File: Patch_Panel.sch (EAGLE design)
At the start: 43 parts, among them M1_IN APP_2POS_CONFIGMOCO_VERT, M1_OUT APP_2POS_CONFIGMOCO_VERT_DUMMY, M2_IN APP_2POS_CONFIGMOCO_VERT, M2_OUT APP_2POS_CONFIGMOCO_VERT_DUMMY, M3_IN APP_2POS_CONFIGMOCO_VERT, M3_OUT APP_2POS_CONFIGMOCO_VERT_DUMMY, M4_IN APP_2POS_CONFIGMOCO_VERT, M4_OUT APP_2POS_CONFIGMOCO_VERT_DUMMY, M5_IN APP_2POS_CONFIGMOCO_VERT, M5_OUT APP_2POS_CONFIGMOCO_VERT_DUMMY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

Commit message: added cutout, rerouted w/ vert app connectors for power in
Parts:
- added U$22, U$29, U$30, U$31, U$32, U$33, U$34, U$35, U$36, U$37, U$38, U$39, U$40, U$41, U$42, U$43, U$44, U$45: APP_MOUTING_WINGVERT, MRDT-Connectors:APP_MOUTING_WINGVERT
- added U$46: RJ45_PASSTHRUSTEWART-SS82000002, MRDT-Connectors:RJ45_PASSTHRUSTEWART-SS82000002
- U$25, U$26: value ANDERSON_POWERPOLEPP45_PCB_VERT -> APP_2POS_CONFIGMOCO_VERT; device MRDT-Connectors:ANDERSON_POWERPOLEPP45_PCB_VERT -> MRDT-Connectors:APP_2POS_CONFIGMOCO_VERT
- U$27, U$28: value ANDERSON_POWERPOLEPP45_PCB_VERT -> APP_MOUTING_WINGVERT; device MRDT-Connectors:ANDERSON_POWERPOLEPP45_PCB_VERT -> MRDT-Connectors:APP_MOUTING_WINGVERT
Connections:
- net 12V: now also U$25VCC.P$1; no longer U$27.P$1
- net 5V: now also U$26VCC.P$1; no longer U$28.P$1
- net GND: now also U$25GND.P$1, U$26GND.P$1; no longer U$25.P$1, U$26.P$1
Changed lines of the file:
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@@
 <part name="SUPPLY4" library="SparkFun-Aesthetics" deviceset="12V" device=""/>
 <part name="GND2" library="SparkFun-Aesthetics" deviceset="GND" device=""/>
-<part name="U$25" library="MRDT-Connectors" deviceset="ANDERSON_POWERPOLE" device="PP45_PCB_VERT"/>
-<part name="U$26" library="MRDT-Connectors" deviceset="ANDERSON_POWERPOLE" device="PP45_PCB_VERT"/>
-<part name="U$27" library="MRDT-Connectors" deviceset="ANDERSON_POWERPOLE" device="PP45_PCB_VERT"/>
-<part name="U$28" library="MRDT-Connectors" deviceset="ANDERSON_POWERPOLE" device="PP45_PCB_VERT"/>
 <part name="U$8" library="MRDT-Connectors" deviceset="APP_3POS_CONFIG" device="5V_12V_VERT"/>
 <part name="U$1" library="MRDT-Connectors" deviceset="APP_3POS_CONFIG" device="5V_12V_VERT"/>
@@
 <part name="U$20" library="MRDT-Connectors" deviceset="APP_3POS_CONFIG" device="5V_12V_VERT"/>
 <part name="U$21" library="MRDT-Connectors" deviceset="APP_3POS_CONFIG" device="5V_12V_VERT"/>
+<part name="U$22" library="MRDT-Connectors" deviceset="APP_MOUTING_WING" device="VERT"/>
+<part name="U$29" library="MRDT-Connectors" deviceset="APP_MOUTING_WING" device="VERT"/>
+<part name="U$30" library="MRDT-Connectors" deviceset="APP_MOUTING_WING" device="VERT"/>
+<part name="U$31" library="MRDT-Connectors" deviceset="APP_MOUTING_WING" device="VERT"/>
+<part name="U$32" library="MRDT-Connectors" deviceset="APP_MOUTING_WING" device="VERT"/>
+<part name="U$33" library="MRDT-Connectors" deviceset="APP_MOUTING_WING" device="VERT"/>
+<part name="U$34" library="MRDT-Connectors" deviceset="APP_MOUTING_WING" device="VERT"/>
+<part name="U$25" library="MRDT-Connectors" deviceset="APP_2POS_CONFIG" device="MOCO_VERT"/>
+<part name="U$26" library="MRDT-Connectors" deviceset="APP_2POS_CONFIG" device="MOCO_VERT"/>
+<part name="U$27" library="MRDT-Connectors" deviceset="APP_MOUTING_WING" device="VERT"/>
+<part name="U$28" library="MRDT-Connectors" deviceset="APP_MOUTING_WING" device="VERT"/>
+<part name="U$35" library="MRDT-Connectors" deviceset="APP_MOUTING_WING" device="VERT"/>
+<part name="U$36" library="MRDT-Connectors" deviceset="APP_MOUTING_WING" device="VERT"/>
+<part name="U$37" library="MRDT-Connectors" deviceset="APP_MOUTING_WING" device="VERT"/>
+<part name="U$38" library="MRDT-Connectors" deviceset="APP_MOUTING_WING" device="VERT"/>
+<part name="U$39" library="MRDT-Connectors" deviceset="APP_MOUTING_WING" device="VERT"/>
+<part name="U$40" library="MRDT-Connectors" deviceset="APP_MOUTING_WING" device="VERT"/>
+<part name="U$41" library="MRDT-Connectors" deviceset="APP_MOUTING_WING" device="VERT"/>
+<part name="U$42" library="MRDT-Connectors" deviceset="APP_MOUTING_WING" device="VERT"/>
+<part name="U$43" library="MRDT-Connectors" deviceset="APP_MOUTING_WING" device="VERT"/>
+<part name="U$44" library="MRDT-Connectors" deviceset="APP_MOUTING_WING" device="VERT"/>
+<part name="U$45" library="MRDT-Connectors" deviceset="APP_MOUTING_WING" device="VERT"/>
+<part name="U$46" library="MRDT-Connectors" deviceset="RJ45_PASSTHRU" device="STEWART-SS82000002"/>
 </parts>
 <sheets>
@@
 <wire x1="228.6" y1="162.56" x2="228.6" y2="91.44" width="0.1524" layer="94" style="shortdash"/>
 <wire x1="228.6" y1="91.44" x2="86.36" y2="91.44" width="0.1524" layer="94" style="shortdash"/>
-<wire x1="86.36" y1="91.44" x2="86.36" y2="-73.66" width="0.1524" layer="94" style="shortdash"/>
-<wire x1="86.36" y1="-73.66" x2="-25.4" y2="-73.66" width="0.1524" layer="94" style="shortdash"/>
-<wire x1="-25.4" y1="-73.66" x2="-25.4" y2="162.56" width="0.1524" layer="94" style="shortdash"/>
+<wire x1="86.36" y1="91.44" x2="86.36" y2="-231.14" width="0.1524" layer="94" style="shortdash"/>
+<wire x1="86.36" y1="-231.14" x2="-25.4" y2="-231.14" width="0.1524" layer="94" style="shortdash"/>
+<wire x1="-25.4" y1="-231.14" x2="-25.4" y2="162.56" width="0.1524" layer="94" style="shortdash"/>
 <text x="-22.86" y="157.48" size="1.778" layer="94">POWER OUT</text>
 </plain>
@@
 <instance part="SUPPLY4" gate="G$1" x="-7.62" y="205.74"/>
 <instance part="GND2" gate="1" x="7.62" y="208.28" rot="R180"/>
-<instance part="U$25" gate="G$1" x="20.32" y="175.26"/>
-<instance part="U$26" gate="G$1" x="20.32" y="190.5"/>
-<instance part="U$27" gate="G$1" x="20.32" y="195.58"/>
-<instance part="U$28" gate="G$1" x="20.32" y="180.34"/>
 <instance part="U$8" gate="GND" x="20.32" y="139.7"/>
 <instance part="U$8" gate="5V" x="20.32" y="144.78"/>
@@
 <instance part="AUX2_OUT" gate="GND" x="210.82" y="149.86" rot="R270"/>
 <instance part="AUX2_OUT" gate="VCC" x="215.9" y="149.86" rot="R270"/>
-<instance part="U$9" gate="G$1" x="93.98" y="83.82"/>
-<instance part="U$10" gate="G$1" x="93.98" y="76.2"/>
+<instance part="U$9" gate="G$1" x="91.44" y="81.28"/>
+<instance part="U$10" gate="G$1" x="91.44" y="73.66"/>
 <instance part="U$11" gate="GND" x="20.32" y="-73.66"/>
 <instance part="U$11" gate="5V" x="20.32" y="-68.58"/>
@@
 <instance part="U$21" gate="5V" x="20.32" y="-210.82"/>
 <instance part="U$21" gate="12V" x="20.32" y="-205.74"/>
+<instance part="U$22" gate="G$1" x="91.44" y="66.04"/>
+<instance part="U$29" gate="G$1" x="104.14" y="66.04"/>
+<instance part="U$30" gate="G$1" x="104.14" y="73.66"/>
+<instance part="U$31" gate="G$1" x="104.14" y="81.28"/>
+<instance part="U$32" gate="G$1" x="116.84" y="81.28"/>
+<instance part="U$33" gate="G$1" x="116.84" y="73.66"/>
+<instance part="U$34" gate="G$1" x="116.84" y="66.04"/>
+<instance part="U$25" gate="GND" x="20.32" y="190.5"/>
+<instance part="U$25" gate="VCC" x="20.32" y="195.58"/>
+<instance part="U$26" gate="GND" x="20.32" y="175.26"/>
+<instance part="U$26" gate="VCC" x="20.32" y="180.34"/>
+<instance part="U$27" gate="G$1" x="91.44" y="58.42"/>
+<instance part="U$28" gate="G$1" x="91.44" y="50.8"/>
+<instance part="U$35" gate="G$1" x="91.44" y="43.18"/>
+<instance part="U$36" gate="G$1" x="104.14" y="43.18"/>
+<instance part="U$37" gate="G$1" x="104.14" y="50.8"/>
+<instance part="U$38" gate="G$1" x="104.14" y="58.42"/>
+<instance part="U$39" gate="G$1" x="116.84" y="58.42"/>
+<instance part="U$40" gate="G$1" x="116.84" y="50.8"/>
+<instance part="U$41" gate="G$1" x="116.84" y="43.18"/>
+<instance part="U$42" gate="G$1" x="91.44" y="35.56"/>
+<instance part="U$43" gate="G$1" x="104.14" y="35.56"/>
+<instance part="U$44" gate="G$1" x="116.84" y="35.56"/>
+<instance part="U$45" gate="G$1" x="91.44" y="27.94"/>
+<instance part="U$46" gate="G$1" x="91.44" y="12.7"/>
 </instances>
 <busses>
@@
 <wire x1="0" y1="-50.8" x2="0" y2="-33.02" width="0.1524" layer="91"/>
 <pinref part="U$8" gate="5V" pin="P$1"/>
-<pinref part="U$28" gate="G$1" pin="P$1"/>
 <wire x1="0" y1="-33.02" x2="0" y2="-15.24" width="0.1524" layer="91"/>
 <wire x1="0" y1="-15.24" x2="0" y2="2.54" width="0.1524" layer="91"/>
@@
 <junction x="0" y="-68.58"/>
 <junction x="0" y="-50.8"/>
-<wire x1="0" y1="-210.82" x2="0" y2="-195.58" width="0.1524" layer="91"/>
+<wire x1="0" y1="-210.82" x2="0" y2="-193.04" width="0.1524" layer="91"/>
 <wire x1="12.7" y1="-210.82" x2="0" y2="-210.82" width="0.1524" layer="91"/>
 <pinref part="U$21" gate="5V" pin="P$1"/>
-<wire x1="0" y1="-195.58" x2="0" y2="-193.04" width="0.1524" layer="91"/>
 <junction x="0" y="-193.04"/>
+<pinref part="U$26" gate="VCC" pin="P$1"/>
 </segment>
 </net>
@@
 <wire x1="12.7" y1="149.86" x2="-7.62" y2="149.86" width="0.1524" layer="91"/>
 <pinref part="U$8" gate="12V" pin="P$1"/>
-<pinref part="U$27" gate="G$1" pin="P$1"/>
 <wire x1="12.7" y1="195.58" x2="-7.62" y2="195.58" width="0.1524" layer="91"/>
 <junction x="-7.62" y="195.58"/>
@@
 <junction x="-7.62" y="-63.5"/>
 <junction x="-7.62" y="-45.72"/>
-<wire x1="-7.62" y1="-205.74" x2="-7.62" y2="-190.5" width="0.1524" layer="91"/>
+<wire x1="-7.62" y1="-205.74" x2="-7.62" y2="-187.96" width="0.1524" layer="91"/>
 <wire x1="12.7" y1="-205.74" x2="-7.62" y2="-205.74" width="0.1524" layer="91"/>
 <pinref part="U$21" gate="12V" pin="P$1"/>
-<wire x1="-7.62" y1="-190.5" x2="-7.62" y2="-187.96" width="0.1524" layer="91"/>
 <junction x="-7.62" y="-187.96"/>
+<pinref part="U$25" gate="VCC" pin="P$1"/>
 </segment>
 </net>
@@
 <wire x1="7.62" y1="139.7" x2="7.62" y2="121.92" width="0.1524" layer="91"/>
 <pinref part="U$8" gate="GND" pin="P$1"/>
-<pinref part="U$25" gate="G$1" pin="P$1"/>
 <wire x1="7.62" y1="121.92" x2="7.62" y2="104.14" width="0.1524" layer="91"/>
 <wire x1="7.62" y1="104.14" x2="7.62" y2="86.36" width="0.1524" layer="91"/>
@@
 <wire x1="7.62" y1="175.26" x2="7.62" y2="139.7" width="0.1524" layer="91"/>
 <junction x="7.62" y="139.7"/>
-<pinref part="U$26" gate="G$1" pin="P$1"/>
 <wire x1="12.7" y1="190.5" x2="7.62" y2="190.5" width="0.1524" layer="91"/>
 <wire x1="7.62" y1="190.5" x2="7.62" y2="175.26" width="0.1524" layer="91"/>
@@
 <junction x="7.62" y="-55.88"/>
 <pinref part="U$21" gate="GND" pin="P$1"/>
-<wire x1="7.62" y1="-200.66" x2="7.62" y2="-215.9" width="0.1524" layer="91"/>
+<wire x1="7.62" y1="-198.12" x2="7.62" y2="-215.9" width="0.1524" layer="91"/>
 <wire x1="12.7" y1="-215.9" x2="7.62" y2="-215.9" width="0.1524" layer="91"/>
-<wire x1="7.62" y1="-200.66" x2="7.62" y2="-198.12" width="0.1524" layer="91"/>
 <junction x="7.62" y="-198.12"/>
+<pinref part="U$26" gate="GND" pin="P$1"/>
+<pinref part="U$25" gate="GND" pin="P$1"/>
 </segment>
 <segment>

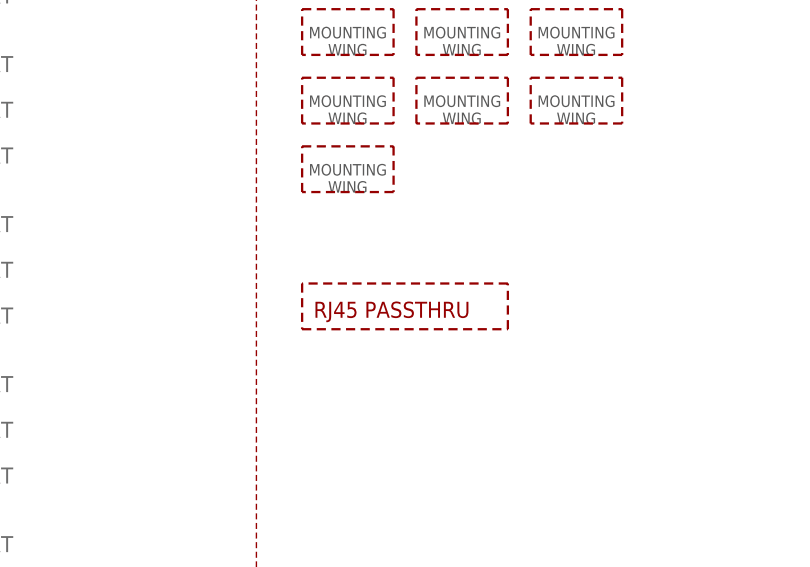
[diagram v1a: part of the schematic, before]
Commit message: added rj45 standoff - needs placed
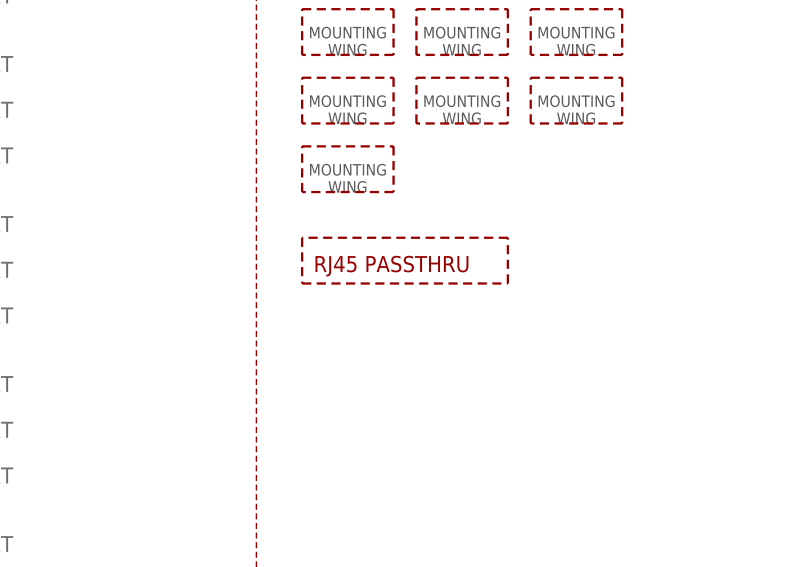
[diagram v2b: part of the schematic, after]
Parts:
- U$46: value RJ45_PASSTHRUSTEWART-SS82000002 -> RJ45_PASSTHRUMRDT_MALE_RJ45_STANDOFF; device MRDT-Connectors:RJ45_PASSTHRUSTEWART-SS82000002 -> MRDT-Connectors:RJ45_PASSTHRUMRDT_MALE_RJ45_STANDOFF
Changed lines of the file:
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@@
 <part name="U$44" library="MRDT-Connectors" deviceset="APP_MOUTING_WING" device="VERT"/>
 <part name="U$45" library="MRDT-Connectors" deviceset="APP_MOUTING_WING" device="VERT"/>
-<part name="U$46" library="MRDT-Connectors" deviceset="RJ45_PASSTHRU" device="STEWART-SS82000002"/>
+<part name="U$46" library="MRDT-Connectors" deviceset="RJ45_PASSTHRU" device="MRDT_MALE_RJ45_STANDOFF"/>
 </parts>
 <sheets>
@@
 <instance part="U$44" gate="G$1" x="116.84" y="35.56"/>
 <instance part="U$45" gate="G$1" x="91.44" y="27.94"/>
-<instance part="U$46" gate="G$1" x="91.44" y="12.7"/>
+<instance part="U$46" gate="G$1" x="91.44" y="17.78"/>
 </instances>
 <busses>

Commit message: github sucks. i changed some stuff
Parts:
- added U$48, U$49, U$50, U$52, U$53, U$54, U$55, U$56, U$57, U$58, U$59, U$61: MOUNTING_HOLE#8, MRDT-Hardware:MOUNTING_HOLE#8
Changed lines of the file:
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@@
 <part name="U$45" library="MRDT-Connectors" deviceset="APP_MOUTING_WING" device="VERT"/>
 <part name="U$46" library="MRDT-Connectors" deviceset="RJ45_PASSTHRU" device="MRDT_MALE_RJ45_STANDOFF"/>
+<part name="U$48" library="MRDT-Hardware" deviceset="MOUNTING_HOLE" device="#8"/>
+<part name="U$49" library="MRDT-Hardware" deviceset="MOUNTING_HOLE" device="#8"/>
+<part name="U$50" library="MRDT-Hardware" deviceset="MOUNTING_HOLE" device="#8"/>
+<part name="U$52" library="MRDT-Hardware" deviceset="MOUNTING_HOLE" device="#8"/>
+<part name="U$53" library="MRDT-Hardware" deviceset="MOUNTING_HOLE" device="#8"/>
+<part name="U$54" library="MRDT-Hardware" deviceset="MOUNTING_HOLE" device="#8"/>
+<part name="U$55" library="MRDT-Hardware" deviceset="MOUNTING_HOLE" device="#8"/>
+<part name="U$56" library="MRDT-Hardware" deviceset="MOUNTING_HOLE" device="#8"/>
+<part name="U$58" library="MRDT-Hardware" deviceset="MOUNTING_HOLE" device="#8"/>
+<part name="U$59" library="MRDT-Hardware" deviceset="MOUNTING_HOLE" device="#8"/>
+<part name="U$57" library="MRDT-Hardware" deviceset="MOUNTING_HOLE" device="#8"/>
+<part name="U$61" library="MRDT-Hardware" deviceset="MOUNTING_HOLE" device="#8"/>
 </parts>
 <sheets>
@@
 <instance part="U$44" gate="G$1" x="116.84" y="35.56"/>
 <instance part="U$45" gate="G$1" x="91.44" y="27.94"/>
-<instance part="U$46" gate="G$1" x="91.44" y="17.78"/>
+<instance part="U$46" gate="G$1" x="91.44" y="12.7"/>
+<instance part="U$48" gate="G$1" x="137.16" y="73.66"/>
+<instance part="U$49" gate="G$1" x="137.16" y="66.04"/>
+<instance part="U$50" gate="G$1" x="149.86" y="81.28"/>
+<instance part="U$52" gate="G$1" x="149.86" y="66.04"/>
+<instance part="U$53" gate="G$1" x="137.16" y="58.42"/>
+<instance part="U$54" gate="G$1" x="162.56" y="66.04"/>
+<instance part="U$55" gate="G$1" x="162.56" y="81.28"/>
+<instance part="U$56" gate="G$1" x="149.86" y="73.66"/>
+<instance part="U$58" gate="G$1" x="137.16" y="81.28"/>
+<instance part="U$59" gate="G$1" x="149.86" y="58.42"/>
+<instance part="U$57" gate="G$1" x="162.56" y="73.66"/>
+<instance part="U$61" gate="G$1" x="91.44" y="5.08"/>
 </instances>
 <busses>
